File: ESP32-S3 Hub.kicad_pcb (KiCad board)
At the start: 6 copper layers, 15 x 30 mm, 56 parts, among them J1 Precidip 853-87-004-20-001101, J10 Precidip 853-87-004-20-001101, J11 7 pin FPC 0.3mm Aces 51688-00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, J12 Precidip 853-87-004-20-001101, J13 TE 3-2363961-0 receptacle, J15 Precidip 853-87-004-20-001101, J16 TE 3-2363961-0 receptacle, J18 Precidip 852-10-004-20-001101, J2 Precidip 853-87-004-20-001101, J3 7 pin FPC 0.3mm Aces 51688-00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, J4 Precidip 853-87-004-20-001101, J5 7 pin FPC 0.3mm Aces 51688-00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, J6 Precidip 853-87-004-20-001101, J7 Precidip 853-87-004-20-001101, J8 7 pin FPC 0.3mm Aces 51688-00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, J9 Precidip 853-87-004-20-001101, SW1 Mitsumi R-667996, SW2 Mitsumi R-667996, U1 ESP32-S3, U2 IS31FL3726A-QFLS4, U3 THVD1420DRLR, Y1 ABM11-40.000MHZ-B1U-T3, 10ppm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

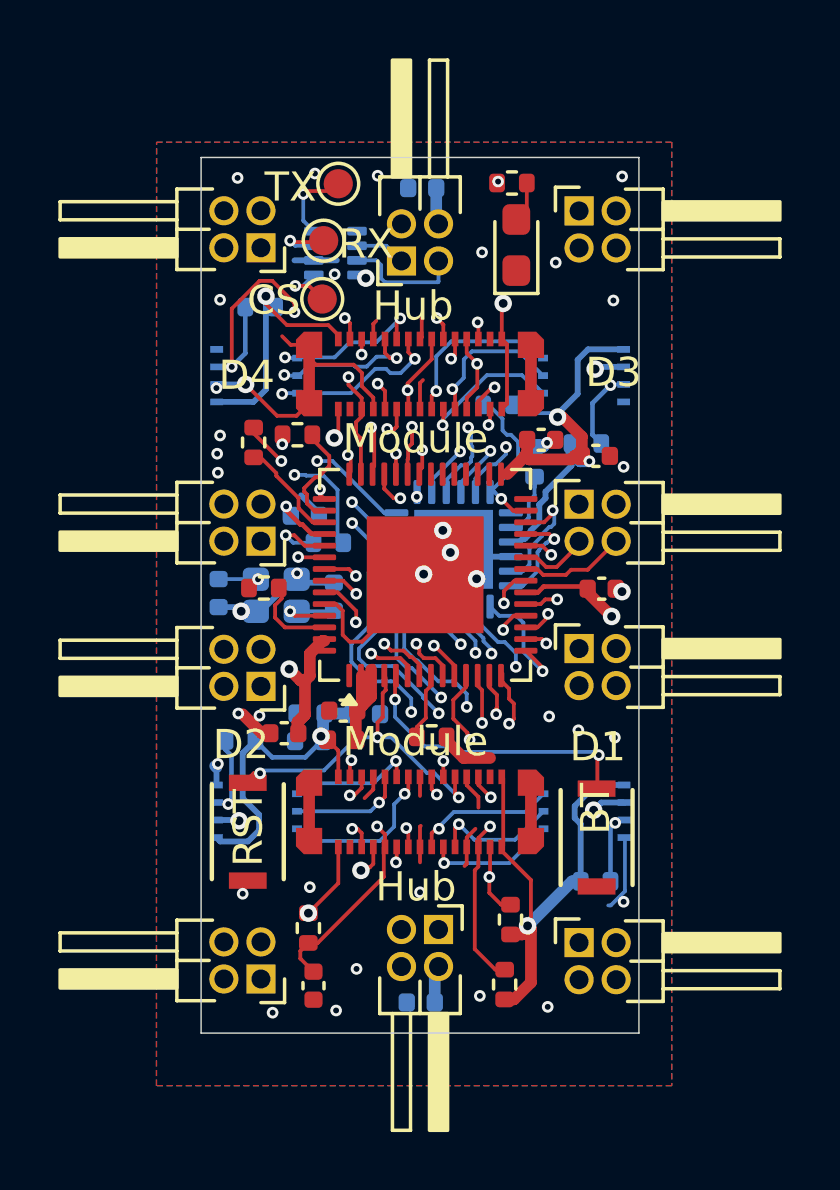
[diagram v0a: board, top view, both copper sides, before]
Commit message: Corrected footprint, started reconnect nets PCB
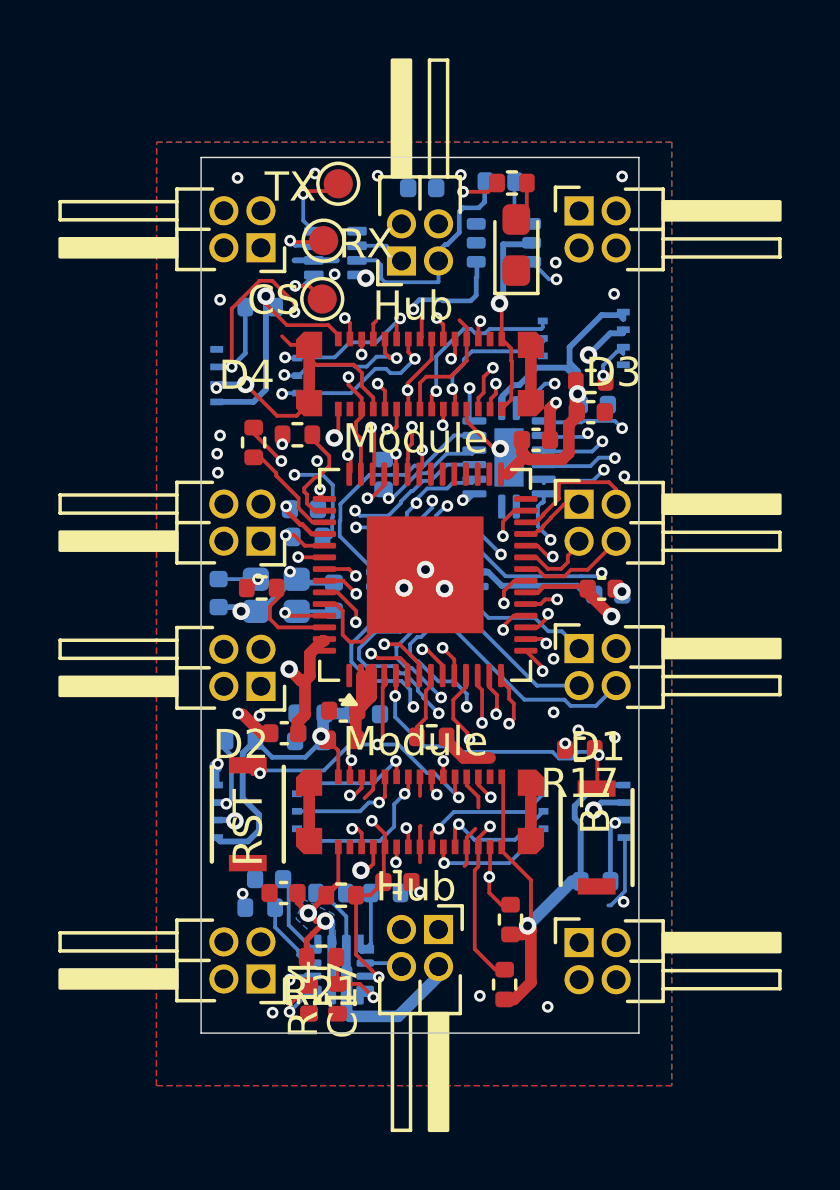
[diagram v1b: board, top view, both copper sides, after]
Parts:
- added C15: 1uF, Capacitor_SMD:C_0402_1005Metric, B.Cu at (161.8, 96.8)
- added C16: 1uF, Capacitor_SMD:C_0402_1005Metric, B.Cu at (161.4, 90.3)
- added C17: 3.3nF, Capacitor_SMD:C_0402_1005Metric, F.Cu at (151.6, 110.7)
- added C18: 2.7nF, Capacitor_SMD:C_0402_1005Metric, B.Cu at (150.2, 106.5)
- added R13: 10k, Resistor_SMD:R_0402_1005Metric, B.Cu at (154.2, 92.7)
- added R14: 100k, Resistor_SMD:R_0402_1005Metric, F.Cu at (152.6, 110.6)
- added R15: 6.04k, Resistor_SMD:R_0402_1005Metric, B.Cu at (149.9, 107.5)
- added R16: 120ohm, Resistor_SMD:R_0402_1005Metric, B.Cu at (158.2, 82.6)
- added R17: 10k, Resistor_SMD:R_0402_1005Metric, F.Cu at (160.9, 102.1)
- added R21: 150k, Resistor_SMD:R_0402_1005Metric, F.Cu at (152.0, 109.2)
- added U4: TPS2521ARPWR, custom_Power_QFN:QFN-10_10VQFN_2x2mm_P0.5mm, B.Cu at (152.6, 109.6)
- added U5: SN74LV595A, Package_DFN_QFN:DHVQFN-16-1EP_2.5x3.5mm_P0.5mm_EP1x2mm, B.Cu at (155.7, 96.2)
- added U6: TS5A3159DCK, Package_TO_SOT_SMD:SOT-363_SC-70-6, B.Cu at (158.3, 84.7)
- C14, R19: moved to F.Cu
- R11: value 10k -> 470k
- R12: value 1.8k -> 332k
- U2: value IS31FL3726A-QFLS4 -> SN74LV595A; footprint Package_DFN_QFN:QFN-24-1EP_4x4mm_P0.5mm_EP2.7x2.7mm -> Package_DFN_QFN:DHVQFN-16-1EP_2.5x3.5mm_P0.5mm_EP1x2mm
- moved R11 17.7 mm to (152.3, 107.0), turned to 180 degrees
- moved R12 15.6 mm to (154.2, 107.0), turned to 180 degrees
- moved C14 6.01 mm to (150.7, 107.0)
- moved C13 4.57 mm to (154.6, 106.6), turned to 0 degrees
- moved U2 3.68 mm to (158.4, 92.1)
- moved R19 2.13 mm to (161.2, 89.5)
- moved R7 1.59 mm to (152.7, 107.1), turned to 180 degrees
- moved C7 1.51 mm to (161.2, 90.5)
- moved J8 1.28 mm to (161.1, 88.0)
- moved R5 0.74 mm to (151.6, 94.8)
- moved SW2 0.60 mm to (149.5, 104.3)
- moved C10 0.23 mm to (151.4, 93.8)
- moved C5 0.18 mm to (159.4, 91.5)
- moved R6 0.08 mm to (150.0, 96.5)
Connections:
- J12 pad 4: VDD -> VBUS
- J18 pad 2: VDD -> VBUS
- R11 pad 1: ShiftEn -> Net-(U4-EN/UVLO)
- R11 pad 2: VDD -> VBUS
- R12 pad 2: Net-(U2-R_EXT) -> Net-(U4-EN/UVLO)
- U1 pad 16: 4CSA-C -> ShiftData
- U1 pad 17: 4CSA-D -> ShiftCLK
- U1 pad 18: 4CSA-B -> 4CSA-D
- U1 pad 19: 3CSA-B -> 4CSA-C
- U1 pad 24: 3CSA-A -> 4CSA-B
- U1 pad 25: ShiftCLK -> 3CSA-A
- U1 pad 26: ShiftData -> 3CSA-B
- U2 pad 1: unconnected-(U2-SERIAL-OUT-Pad1) -> 4A
- U2 pad 10: 1C -> VDD
- U2 pad 11: 1D -> ShiftCLK
- U2 pad 12: 2B -> ShiftLatch
- U2 pad 13: 2D -> ShiftEn
- U2 pad 14: 2A -> Net-(U2-SER)
- U2 pad 15: 2C -> 4B
- U2 pad 16: 4B -> VDD
- U2 pad 17: 4A -> GND
- U2 pad 2: Net-(U2-R_EXT) -> 4D
- U2 pad 3: VDD -> 4C
- U2 pad 4: GND -> 3A
- U2 pad 5: ShiftData -> 3B
- U2 pad 6: ShiftCLK -> 3D
- U2 pad 7: ShiftLatch -> 3C
- U2 pad 8: 1B -> GND
- U2 pad 9: 1A -> unconnected-(U2-QH&apos;-Pad9)
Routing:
- net VBUS: track 0.00 -> 40.4 mm
- net VDD: track 80.2 -> 89.9 mm, vias 12 -> 15
- net Net-(U2-SER): track 0.00 -> 8.49 mm
- net 4CSA-C: track 21.6 -> 14.3 mm
- net UART0_TX: track 43.9 -> 50.9 mm
- net 4CSA-D: track 23.1 -> 16.3 mm
- net 4CSA-B: track 19.7 -> 13.6 mm
- net 4CSA-A: track 18.4 -> 12.4 mm
- net 3B: track 16.2 -> 11.0 mm
- net UART0_RX: track 33.9 -> 39.1 mm
- net 3CSA-B: track 9.05 -> 4.59 mm, vias 1 -> 0
- net RS485-: track 31.3 -> 35.6 mm, vias 0 -> 1
- net CS1: track 23.3 -> 19.2 mm
- net CS2: track 28.1 -> 24.1 mm
- net SDA1: track 42.4 -> 38.8 mm
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- added copper zone on In2.Cu, net GND
- added copper zone on B.Cu, net VDD
- added copper zone on In4.Cu, net VDD
- removed copper zone on In4.Cu, net GND
- removed copper zone on In2.Cu, net VDD
